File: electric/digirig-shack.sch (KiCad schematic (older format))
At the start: 61 parts, among them J1 USB_B_Micro, J2 USB_A, J3 PTT/CW, J4 Serial, J5 Audio, T1 600/600 Audio, T2 600/600 Audio, U1 TUSB2046, U2 CM108, U3 CP2102N-A01, U4 PC817, U5 PC817, Y1 6MHz, Y2 12MHz

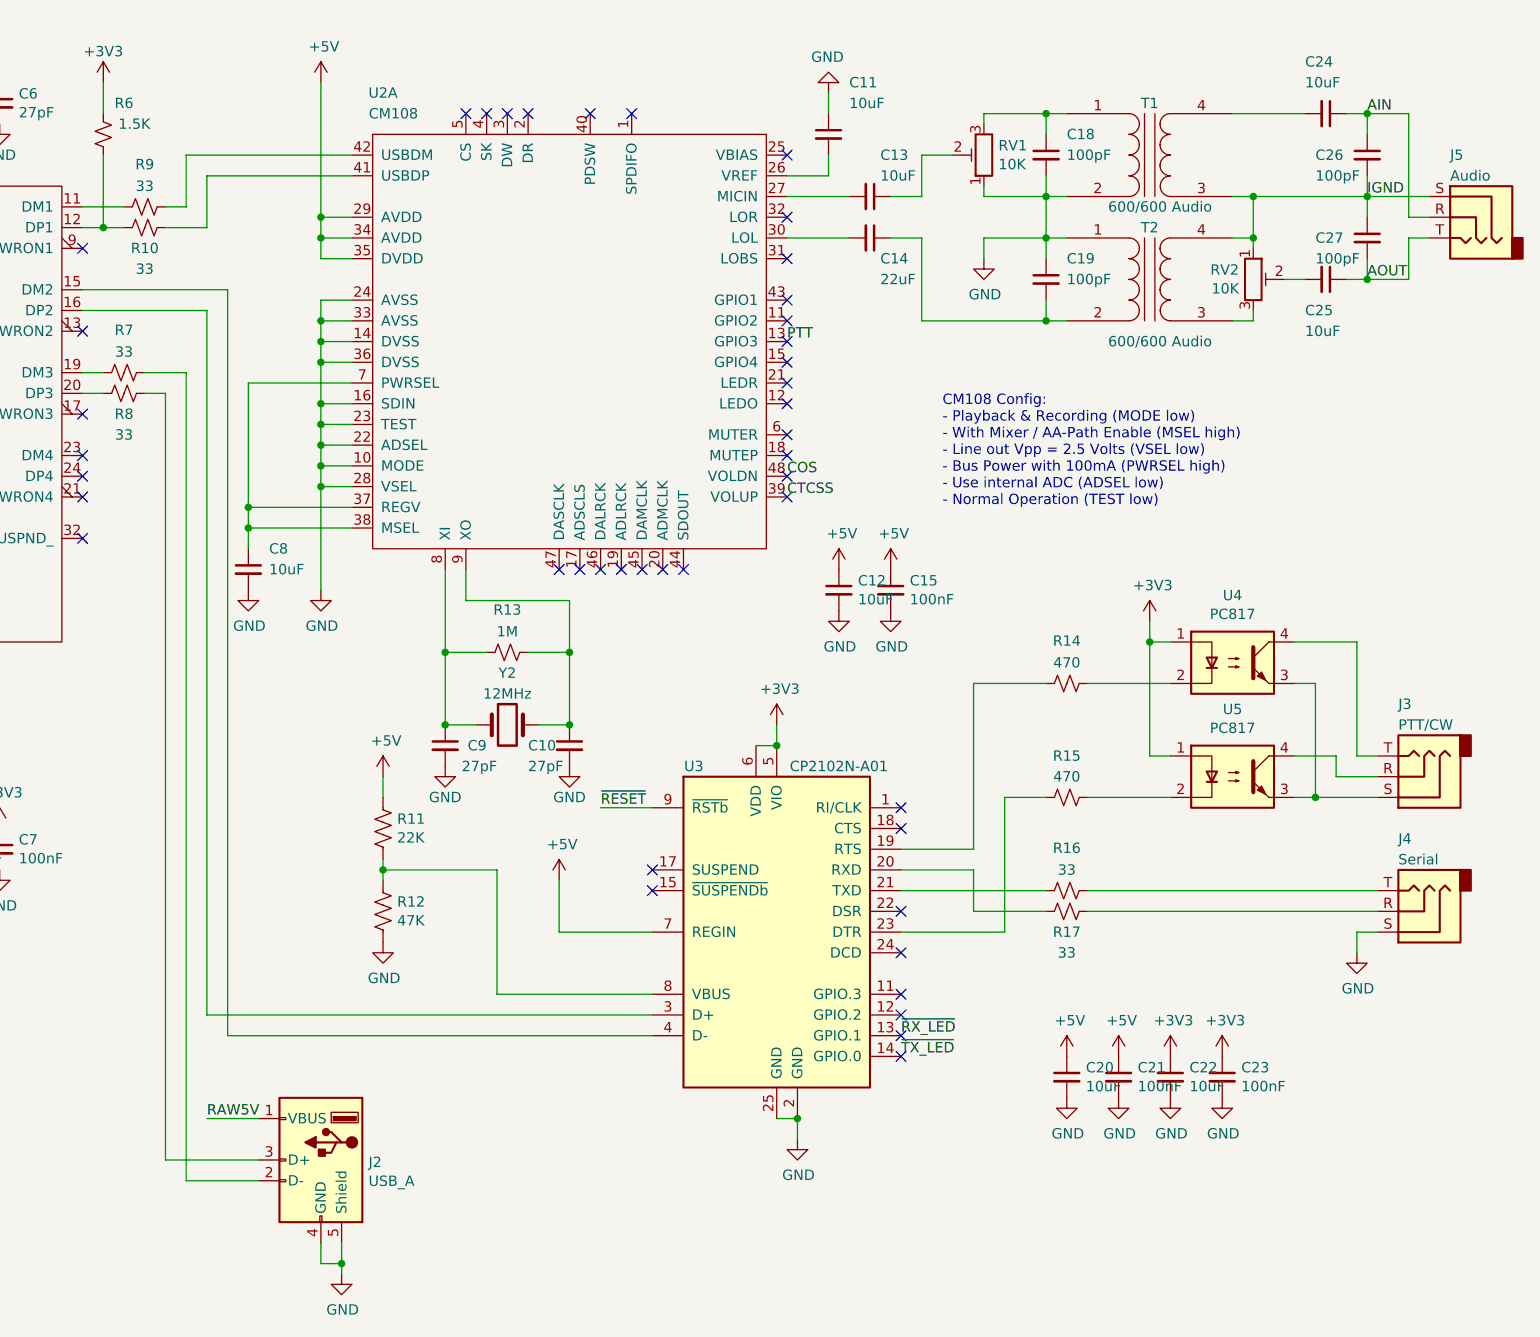
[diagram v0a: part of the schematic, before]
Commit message: Rev 1.1 Mods Continued
Compressed mobile version to 23mm width
Added pulldown resistors on secondary USB ports in shack version
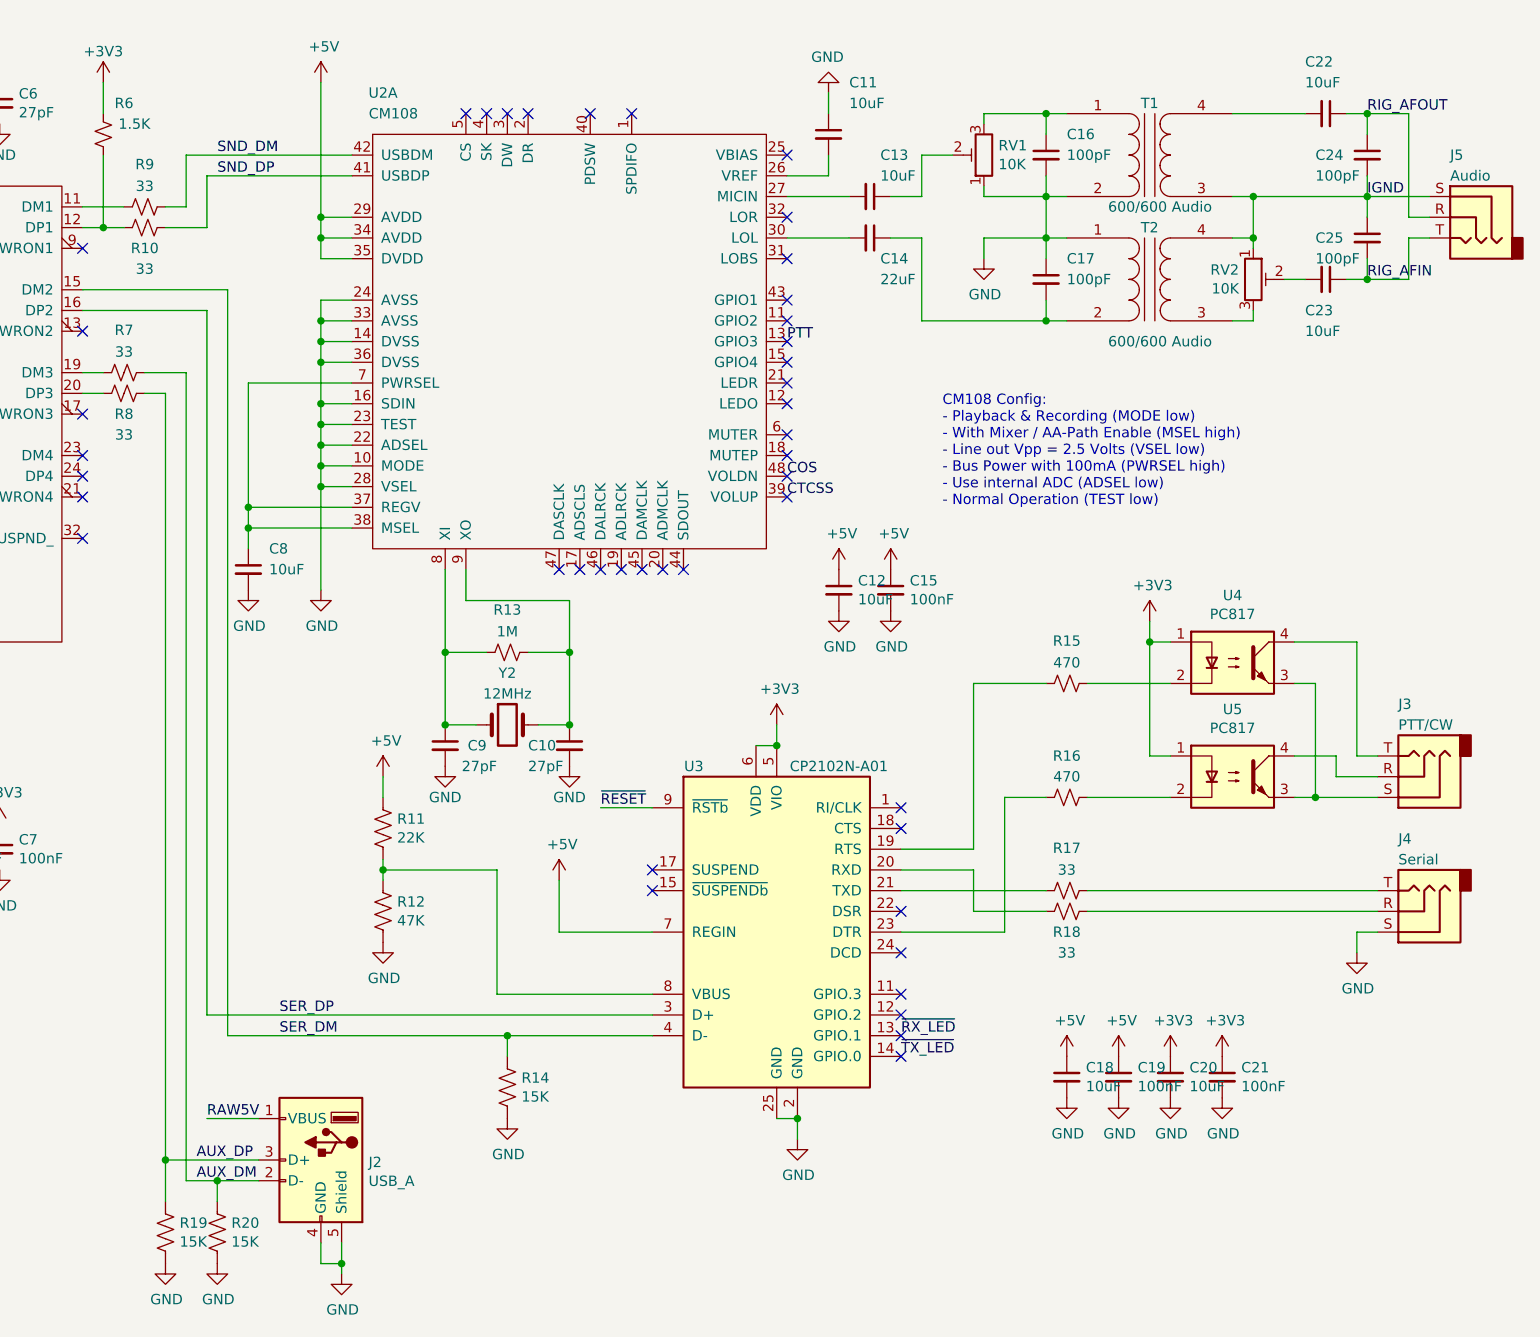
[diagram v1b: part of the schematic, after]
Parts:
- added R14, R19, R20: 15K, Resistor_SMD:R_0402_1005Metric, symbol Device:R_US
- renumbered C18 to C16, C19 to C17, C20 to C18, C21 to C19, C22 to C20, C23 to C21, C24 to C22, C25 to C23, C26 to C24, C27 to C25, R14 to R15, R15 to R16, R16 to R17, R17 to R18
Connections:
- net GND: now also R14.2, R19.2, R20.2
- net SER_DM: now reaches U1.15 (DM2), U3.4 (D-)
- net SER_DM: now also R14.1
- net SER_DP: now reaches U1.16 (DP2), U3.3 (D+)
- net AUX_DM: now reaches J2.2 (D-), R7.1
- net AUX_DM: now also R20.1
- net AUX_DP: now reaches J2.3 (D+), R8.1
- net AUX_DP: now also R19.1
- net SND_DP: now reaches R10.1, U2.41 (USBDP)
- net SND_DM: now reaches R9.1, U2.42 (USBDM)
- net AIN renamed RIG_AFOUT
- net AOUT renamed RIG_AFIN

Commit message: Revision 1.3 updates
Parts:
- added H1, H2, H3, H4: M3, MountingHole:MountingHole_3.2mm_M3_Pad_Via, symbol Mechanical:MountingHole_Pad
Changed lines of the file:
@@
 Text Label 4850 1400 0    50   ~ 0
 SND_DP
+$Comp
+L Mechanical:MountingHole_Pad H1
+U 1 1 6017CD19
+P 1500 6500
+F 0 "H1" H 1600 6549 50  0000 L CNN
+F 1 "M3" H 1600 6458 50  0000 L CNN
+F 2 "MountingHole:MountingHole_3.2mm_M3_Pad_Via" H 1500 6500 50  0001 C CNN
+F 3 "~" H 1500 6500 50  0001 C CNN
+	1    1500 6500
+	1    0    0    -1
+$EndComp
+$Comp
+L power:GND #PWR054
+U 1 1 6017E5B4
+P 1500 6600
+F 0 "#PWR054" H 1500 6350 50  0001 C CNN
+F 1 "GND" H 1505 6427 50  0000 C CNN
+F 2 "" H 1500 6600 50  0001 C CNN
+F 3 "" H 1500 6600 50  0001 C CNN
+	1    1500 6600
+	1    0    0    -1
+$EndComp
+$Comp
+L Mechanical:MountingHole_Pad H2
+U 1 1 6018D2E2
+P 1800 6500
+F 0 "H2" H 1900 6549 50  0000 L CNN
+F 1 "M3" H 1900 6458 50  0000 L CNN
+F 2 "MountingHole:MountingHole_3.2mm_M3_Pad_Via" H 1800 6500 50  0001 C CNN
+F 3 "~" H 1800 6500 50  0001 C CNN
+	1    1800 6500
+	1    0    0    -1
+$EndComp
+$Comp
+L power:GND #PWR055
+U 1 1 6018D4E4
+P 1800 6600
+F 0 "#PWR055" H 1800 6350 50  0001 C CNN
+F 1 "GND" H 1805 6427 50  0000 C CNN
+F 2 "" H 1800 6600 50  0001 C CNN
+F 3 "" H 1800 6600 50  0001 C CNN
+	1    1800 6600
+	1    0    0    -1
+$EndComp
+$Comp
+L Mechanical:MountingHole_Pad H3
+U 1 1 6019CC55
+P 2100 6500
+F 0 "H3" H 2200 6549 50  0000 L CNN
+F 1 "M3" H 2200 6458 50  0000 L CNN
+F 2 "MountingHole:MountingHole_3.2mm_M3_Pad_Via" H 2100 6500 50  0001 C CNN
+F 3 "~" H 2100 6500 50  0001 C CNN
+	1    2100 6500
+	1    0    0    -1
+$EndComp
+$Comp
+L power:GND #PWR056
+U 1 1 6019CE71
+P 2100 6600
+F 0 "#PWR056" H 2100 6350 50  0001 C CNN
+F 1 "GND" H 2105 6427 50  0000 C CNN
+F 2 "" H 2100 6600 50  0001 C CNN
+F 3 "" H 2100 6600 50  0001 C CNN
+	1    2100 6600
+	1    0    0    -1
+$EndComp
+$Comp
+L Mechanical:MountingHole_Pad H4
+U 1 1 601ABF2E
+P 2400 6500
+F 0 "H4" H 2500 6549 50  0000 L CNN
+F 1 "M3" H 2500 6458 50  0000 L CNN
+F 2 "MountingHole:MountingHole_3.2mm_M3_Pad_Via" H 2400 6500 50  0001 C CNN
+F 3 "~" H 2400 6500 50  0001 C CNN
+	1    2400 6500
+	1    0    0    -1
+$EndComp
+$Comp
+L power:GND #PWR057
+U 1 1 601AC164
+P 2400 6600
+F 0 "#PWR057" H 2400 6350 50  0001 C CNN
+F 1 "GND" H 2405 6427 50  0000 C CNN
+F 2 "" H 2400 6600 50  0001 C CNN
+F 3 "" H 2400 6600 50  0001 C CNN
+	1    2400 6600
+	1    0    0    -1
+$EndComp
 $EndSCHEMATC

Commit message: rough draft
- added custom symbols
- first schematic draft
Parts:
- removed C10, C3, C6, C9: 27pF, Capacitor_SMD:C_0402_1005Metric, symbol Device:C_Small
- removed C11, C12, C13, C22, C23, C5, C8: 10uF, Capacitor_SMD:C_0402_1005Metric, symbol Device:C_Small
- removed C14: 22uF, Capacitor_SMD:C_0402_1005Metric, symbol Device:C_Small
- removed C15, C7: 100nF, Capacitor_SMD:C_0402_1005Metric, symbol Device:C_Small
- removed C16, C17, C24, C25: 100pF, Capacitor_SMD:C_0402_1005Metric, symbol Device:C_Small
- removed D1: SP0503BAHT, Package_TO_SOT_SMD:SOT-143, symbol Power_Protection:SP0503BAHT
- removed D2: PWR (RED), LED_SMD:LED_0402_1005Metric, symbol Device:LED
- removed J1: USB_B_Micro, footprints:USB_MICRO_A01SB141B1-298, symbol Connector:USB_B_Micro
- removed J2: USB_A, Connector_USB:USB_A_Molex_67643_Horizontal, symbol Connector:USB_A
- removed J3: PTT/CW, footprints:jack_3.5_pj313d-smt, symbol Connector:AudioJack3
- removed J4: Serial, footprints:jack_3.5_pj313d-smt, symbol Connector:AudioJack3
- removed J5: Audio, footprints:jack_3.5_pj313d-smt, symbol Connector:AudioJack3
- removed L1: 2.2mH, footprints:CD74R, symbol Device:L_Core_Ferrite
- removed R10, R17, R18, R7, R8, R9: 33, Resistor_SMD:R_0402_1005Metric, symbol Device:R_Small_US
- removed R11: 22K, Resistor_SMD:R_0402_1005Metric, symbol Device:R_US
- removed R12: 47K, Resistor_SMD:R_0402_1005Metric, symbol Device:R_US
- removed R13: 1M, Resistor_SMD:R_0402_1005Metric, symbol Device:R_Small_US
- removed R14, R19, R20: 15K, Resistor_SMD:R_0402_1005Metric, symbol Device:R_US
- removed R2: 1K, Resistor_SMD:R_0402_1005Metric, symbol Device:R_Small_US
- removed R5, R6: 1.5K, Resistor_SMD:R_0402_1005Metric, symbol Device:R_Small_US
- removed RV1, RV2: 10K, Potentiometer_SMD:Potentiometer_Bourns_TC33X_Vertical, symbol Device:R_POT_TRIM
- removed T1, T2: 600/600 Audio, footprints:Audio_Transformer, symbol Device:Transformer_1P_1S
- removed U1: TUSB2046, Package_QFP:LQFP-32_7x7mm_P0.8mm, symbol components:TUSB2046
- removed U2: CM108, Package_QFP:LQFP-48_7x7mm_P0.5mm, symbol components:CM108
- removed Y1: 6MHz, Crystal:Crystal_SMD_HC49-SD, symbol Device:Crystal
- removed Y2: 12MHz, Crystal:Crystal_SMD_HC49-SD, symbol Device:Crystal
- added C? (x9): 10uF, Capacitor_SMD:C_0402_1005Metric, symbol Device:C_Small
- added C? (x4): 100nF, Capacitor_SMD:C_0402_1005Metric, symbol Device:C_Small
- added C? (x10): 47pF, Capacitor_SMD:C_0402_1005Metric, symbol Device:C_Small
- added C? (x2): 27pF, Capacitor_SMD:C_0402_1005Metric, symbol Device:C_Small
- added J?: USB_B, symbol Connector:USB_B
- added J?: RJ45_LED_Shielded, symbol Connector:RJ45_LED_Shielded
- added J??: Socket_20DIP, symbol components:Socket_20DIP
- added L?: L_Core_Ferrite, symbol Device:L_Core_Ferrite
- added L?: LOGO, footprints:digirig-logo-6mm, symbol components:LOGO
- added PS?: B0505S-1WR2, CONV_B0505S-1WR2, symbol components:B0505S-1WR2
- added R?: 22K, Resistor_SMD:R_0402_1005Metric, symbol Device:R_Small_US
- added R?: 10K, Resistor_SMD:R_0402_1005Metric, symbol Device:R_Small_US
- added R?: 47K, Resistor_SMD:R_0402_1005Metric, symbol Device:R_Small_US
- added R? (x2): 33, Resistor_SMD:R_0402_1005Metric, symbol Device:R_Small_US
- added R? (x3): 100K, Resistor_SMD:R_0402_1005Metric, symbol Device:R_Small_US
- added R?: 1M, Resistor_SMD:R_0402_1005Metric, symbol Device:R_Small_US
- added R?: 12K, Resistor_SMD:R_0402_1005Metric, symbol Device:R_Small_US
- added R?: 1.5K, Resistor_SMD:R_0402_1005Metric, symbol Device:R_Small_US
- added TP?: CUST, symbol Connector:TestPoint
- added TP?: GPIO3, symbol Connector:TestPoint
- added TP?: GPIO2, symbol Connector:TestPoint
- added TP?: ~RTS, symbol Connector:TestPoint
- added TP?: ~DTR, symbol Connector:TestPoint
- added TP?: COS, symbol Connector:TestPoint
- added TP?: CTCSS, symbol Connector:TestPoint
- added TP?: GPIO4, symbol Connector:TestPoint
- added TP?: GPIO5, symbol Connector:TestPoint
- added TP?: GPIO6, symbol Connector:TestPoint
- added U?: ADUM3160, Package_SO:SOIC-16W_7.5x10.3mm_P1.27mm, symbol Interface_USB:ADUM3160
- added U? (x2), U??: ESDU5V0H4, Package_TO_SOT_SMD:SOT-23-6, symbol components:ESDU5V0H4
- added U?: USB2412-DZK-TR, symbol components:USB2412-DZK-TR
- added U??: CM118B, symbol components:CM118B
- added Y?: 24MHz, Crystal:Crystal_SMD_HC49-SD, symbol Device:Crystal
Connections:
- net labels added: +5P, AFIN_LEFT, AFIN_RIGHT, AFOUT_LEFT, AFOUT_RIGHT, GND1, GND2, PC_5V, PC_DM, PC_DP, PC_GND, RIG_AFIN1, RIG_AFOUT2, RIG_RxD, RIG_TxD, RxD, SRL_DM, SRL_DP, TxD, UL_DM, UL_DP, ~DTR, ~KEY, ~PTT, ~RTS
- net labels removed: AUX_DM, AUX_DP, COS, CTCSS, DM_RAW, DP_RAW, IGND, PTT, RAW5V, RIG_AFIN, RIG_AFOUT, SER_DM, SER_DP
- wire segments 223 -> 355
- no-connect marks 45 -> 41
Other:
- note added: "CM118B Config\n- Bus Power with 100mA (PWRSEL high, PU)\n- Headset Mode: Playback & Recording (MODE low, PD)\n- Normal Operation (TEST low, PD)\n- Headset Topology (MICONLY high, PU)\n- With AA Mixer, Default Mute (MSEL high, PU)"
- note added: "PC Isolation"
- note added: "Serial Interface"
- note added: "Sound Card"
- note added: "TODO:\n- add USB and rig side protection\n- check SPD input on isolator\n- check D-STAR integration options\n- HF filter on the rig side\n- inductor value"
- note added: "USB Hub"
- note added: "USB1412 Config:\n- both ports are non-removable\n (NON_REM1, SUSP_IND/NON_REM2 high at reset)\n- no high speed LED\n (HS_IND low)"
- note removed: "CM108 Config:\n- Playback & Recording (MODE low)\n- With Mixer / AA-Path Enable (MSEL high)\n- Line out Vpp = 2.5 Volts (VSEL low)\n- Bus Power with 100mA (PWRSEL high)\n- Use internal ADC (ADSEL low)\n- Normal Operation (TEST low)"
- note removed: "TUSB2046 Config:\n- Local Power (BUSPWR low, OVERCURx high)\n- Ganged Mode (GANG high)\n- No external memory (EXTMEM high, EECLK nc)\n- Intarnal oscillator (TSTMODE, TSTPLL low)"
- moved on the sheet: C1, C18, C19, C2, C20, C21, C4, R1, R15, R16, R3, R4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

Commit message: Digirig Shack Rev 1.1
- 51mm wide board for sized aluminum case
- electric insulation on PC side instead of audio transformers
- Full size USB B connector on PC side
- RJ45 connector on rig side
- DIP socket for connector pinout configuration
- additional audio and serial pins as headers
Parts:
- removed H1, H2, H3, H4: M3, MountingHole:MountingHole_3.2mm_M3_Pad_Via, symbol Mechanical:MountingHole_Pad
- removed L?: L_Core_Ferrite, symbol Device:L_Core_Ferrite
- added R7, R8: 470, Resistor_SMD:R_0402_1005Metric, symbol Device:R_Small_US
- added TP11, TP12: GND, TestPoint:TestPoint_THTPad_D2.0mm_Drill1.0mm, symbol Connector:TestPoint
- J1: renamed from J?; footprint (none) -> Connector_USB:USB_B_OST_USB-B1HSxx_Horizontal
- J2: renamed from J??; footprint (none) -> Package_DIP:DIP-20_W7.62mm_Socket_LongPads
- J3: renamed from J?; footprint (none) -> Connector_RJ:RJ45_Amphenol_RJHSE538X
- PS1: renamed from PS?; footprint CONV_B0505S-1WR2 -> footprints:CONV_B0505S-1WR2
- TP1, TP10, TP2, TP3, TP4, TP5, TP6, TP7, TP8, TP9: renamed from TP?; footprint (none) -> TestPoint:TestPoint_THTPad_D2.0mm_Drill1.0mm
- U2: renamed from U3; symbol Interface_USB:CP2102N-A01-GQFN24 -> components:CP2102N-A01-GQFN24
- U3: renamed from U?; symbol Interface_USB:ADUM3160 -> components:ADUM3160
- U7: renamed from U?; footprint (none) -> Package_DFN_QFN:QFN-28-1EP_5x5mm_P0.5mm_EP3.35x3.35mm
- U8: renamed from U??; footprint (none) -> Package_QFP:LQFP-48_7x7mm_P0.5mm
- gave numbers to parts that had none: 41
- renumbered C19 to C11, C20 to C14, C21 to C16, C1 to C17, C2 to C20, C4 to C21, C18 to C6, R1 to R10, U4 to U5, U5 to U6
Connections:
- net labels added: PC_N, PC_P, RIG_AFIN2, RIG_AFOUT1, SND_N, SND_P, SRL_N, SRL_P, UL_N, UL_P
- net labels removed: PC_DM, PC_DP, SND_DM, SND_DP, SRL_DM, SRL_DP, UL_DM, UL_DP
- wire segments 355 -> 363
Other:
- note added: "Rig Breakout"
- note removed: "TODO:\n- add USB and rig side protection\n- check SPD input on isolator\n- check D-STAR integration options\n- HF filter on the rig side\n- inductor value"
